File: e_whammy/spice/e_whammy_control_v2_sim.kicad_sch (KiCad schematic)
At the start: 29 parts, among them Q1 NMOS, U1 ${SIM.PARAMS}, U2 ${SIM.PARAMS}, U3 ADG779, U4 OPEN_COLLECTOR_COMPARATOR, U5 OPEN_COLLECTOR_COMPARATOR

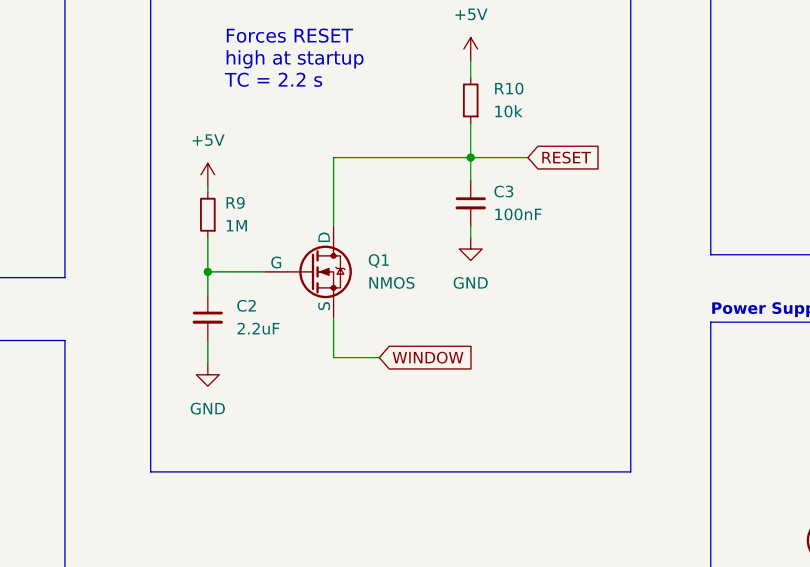
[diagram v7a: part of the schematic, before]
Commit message: e-Whammy v2 sim: model Q1 as 2N7002 startup gate
Replace Q1's bare default VDMOS with the named 2N7002 library model
(Vgs(th) ~2.1 V). The old default only acquired startup because ngspice's
default VDMOS happens to sit near VCC/2; a realistic logic-level FET breaks it.
Q1 is the non-critical startup-reset switch (out of the signal path), so only
the threshold matters. Sim still reproduces plot14; startup acquires ~1.02 s.
Bumps pcb_common for the 2N7002 model.
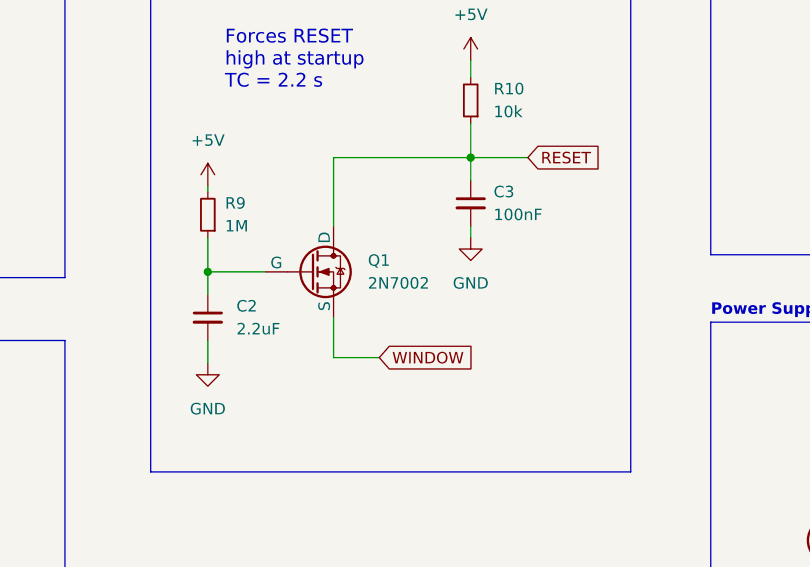
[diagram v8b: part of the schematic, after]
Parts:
- Q1: value NMOS -> 2N7002
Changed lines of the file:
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@@
 			)
 		)
-		(property "Value" "NMOS"
+		(property "Value" "2N7002"
 			(at 197.485 125.0949 0)
 			(effects
@@
 			(effects
 				(font
+					(size 1.27 1.27)
+				)
+				(hide yes)
+			)
+		)
+		(property "Sim.Name" "2N7002"
+			(at 191.135 144.78 0)
+			(effects
+				(font
+					(size 1.27 1.27)
+				)
+				(hide yes)
+			)
+		)
+		(property "Sim.Library" "${KIPRJMOD}/../../pcb_common/kicad/cycfi_spice_library.sp"
+			(at 191.135 146.685 0)
+			(effects
+				(font
